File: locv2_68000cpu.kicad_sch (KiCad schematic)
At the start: 38 parts, among them IC10 93LC66, IC2 68HC000, IC3 ASIC_S0089-1_CF30192X

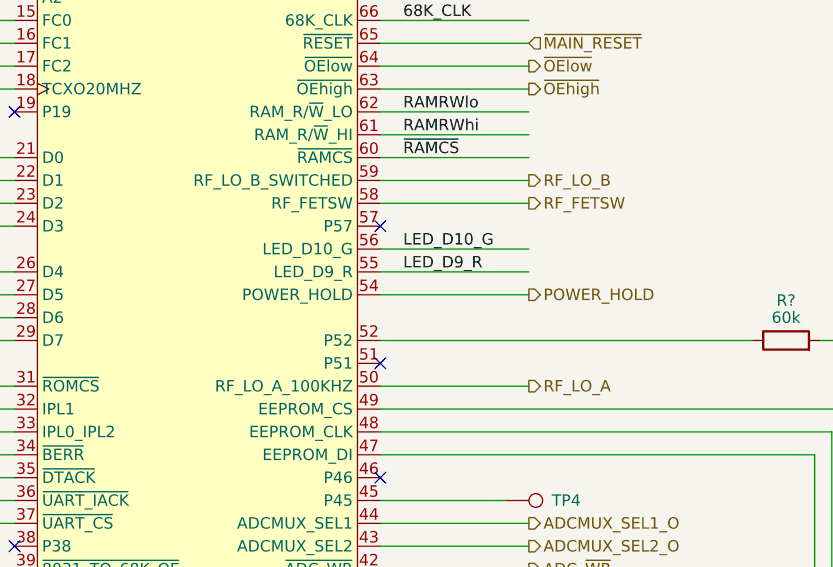
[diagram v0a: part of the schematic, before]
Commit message: Rev B: Fix: Fixed/Variable LO swapped at SA605
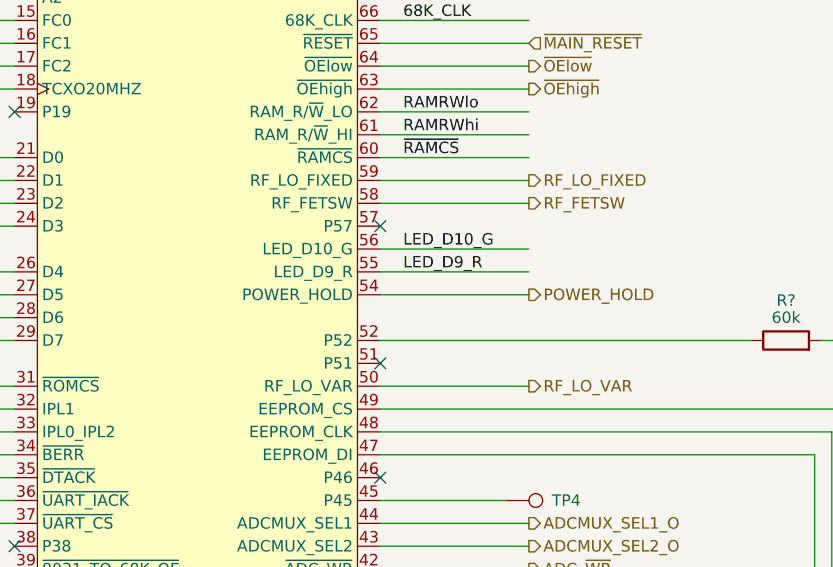
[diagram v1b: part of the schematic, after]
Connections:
- net RF_LO_A renamed RF_LO_VAR
- net RF_LO_B renamed RF_LO_FIXED
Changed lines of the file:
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@@
   (title_block
     (title "Datatrak Locator Mk.2 - 68000 CPU and ASIC")
-    (date "2022-06-29")
-    (rev "A")
+    (date "2022-07-08")
+    (rev "B")
   )
   (junction (at 372.745 198.12) (diameter 0) (color 0 0 0 0)
@@
     (effects (font (size 1.27 1.27)) (justify left))
   )
-  (hierarchical_label "RF_LO_A" (shape output) (at 215.9 124.46 0)
+  (hierarchical_label "RF_LO_VAR" (shape output) (at 215.9 124.46 0)
     (effects (font (size 1.27 1.27)) (justify left))
   )
@@
     (effects (font (size 1.27 1.27)) (justify left))
   )
-  (hierarchical_label "RF_LO_B" (shape output) (at 215.9 101.6 0)
+  (hierarchical_label "RF_LO_FIXED" (shape output) (at 215.9 101.6 0)
     (effects (font (size 1.27 1.27)) (justify left))
   )
